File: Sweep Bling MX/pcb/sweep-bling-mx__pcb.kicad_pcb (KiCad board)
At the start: 2 copper layers, 113.5 x 95.2 mm, 31 parts, among them J2 AudioJack4dpb, SW10 SW_Push, SW11 SW_Push, SW12 SW_Push, SW14 SW_Push, SW15 SW_Push, SW16 SW_Push, SW17 SW_Push, SW18 SW_Push, SW2 SW_Push, SW20 SW_Push, SW21 SW_Push, SW3 SW_Push, SW4 SW_Push, SW5 SW_Push, SW6 SW_Push, SW8 SW_Push, SW9 SW_Push, U1 ProMicro-kbd

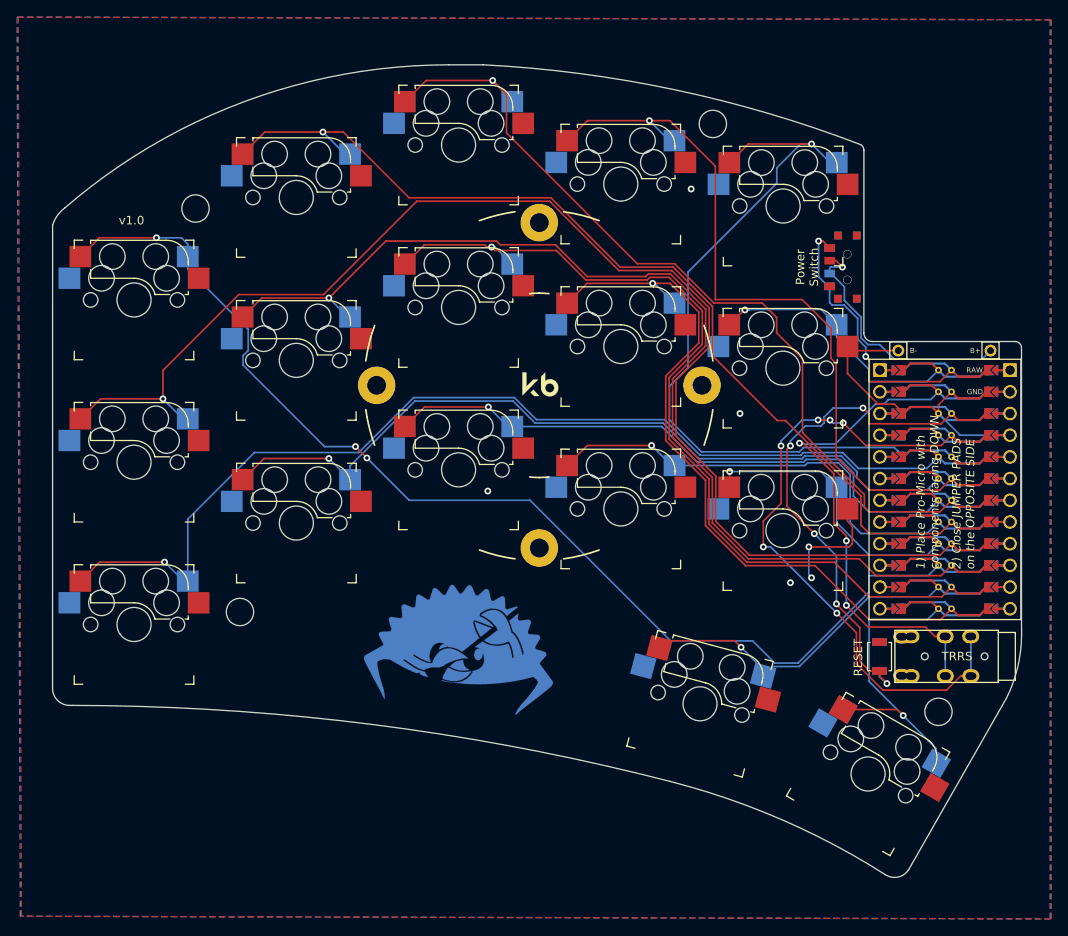
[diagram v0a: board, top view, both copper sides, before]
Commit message: Fix bling mx malformed outline
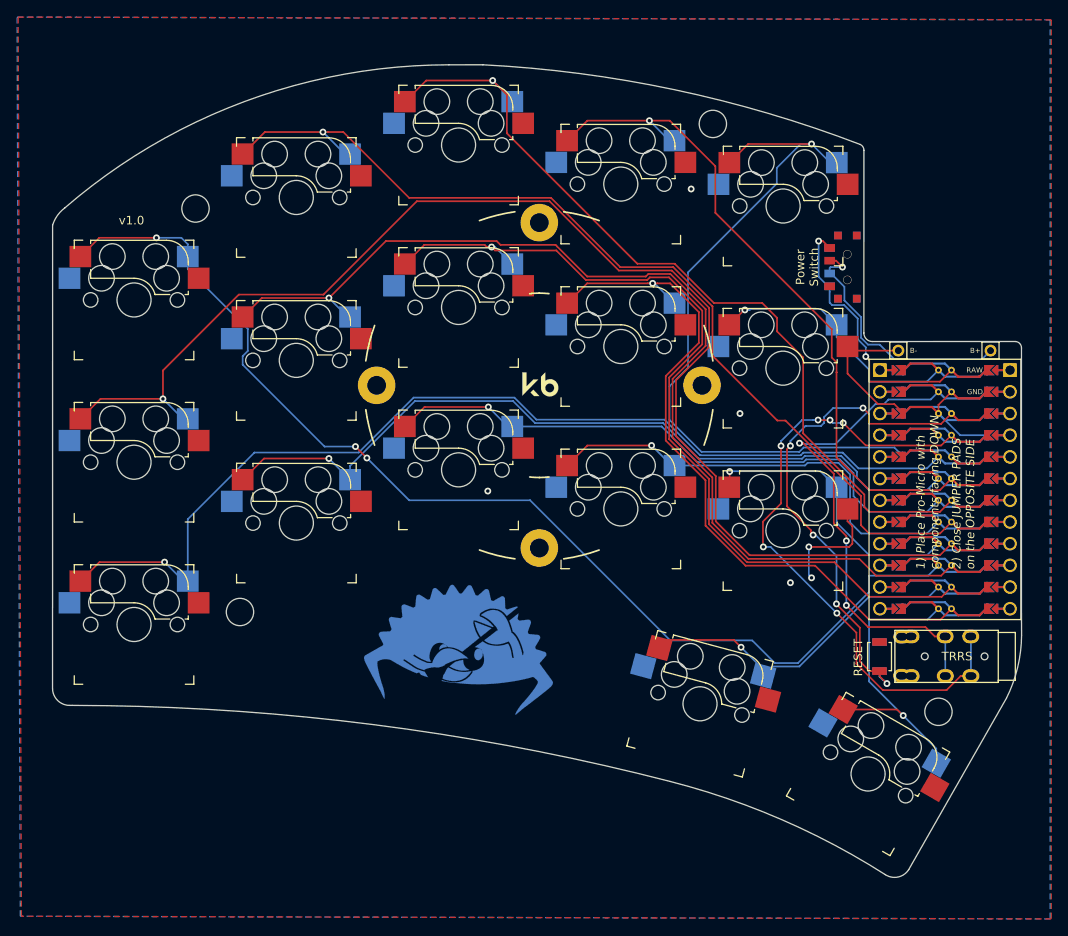
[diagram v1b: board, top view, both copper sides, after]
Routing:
- net Switch4: track 86.0 -> 80.0 mm
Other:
- net class Default removed
